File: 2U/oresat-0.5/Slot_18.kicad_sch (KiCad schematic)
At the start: 3 parts

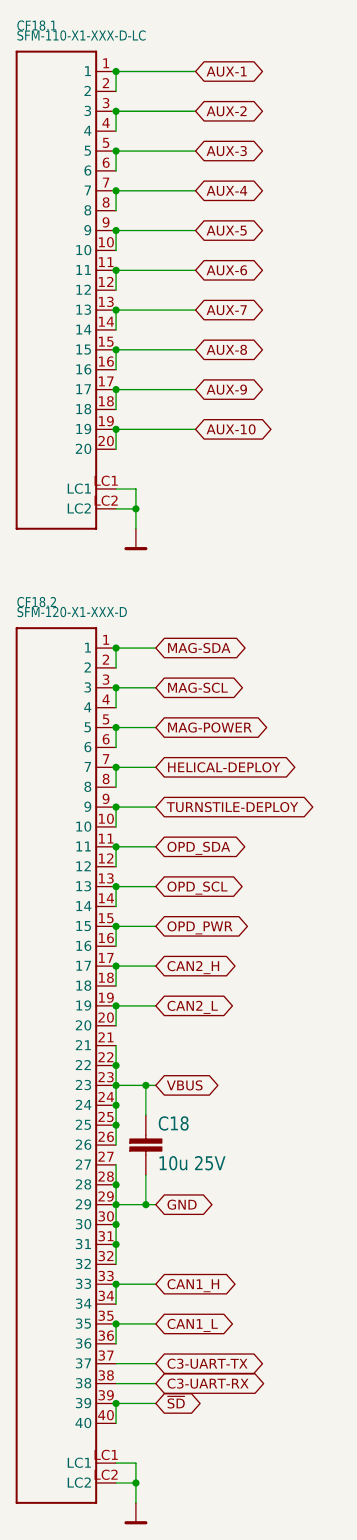
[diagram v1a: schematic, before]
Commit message: Fixed all (most) of the issues from Eagle imports
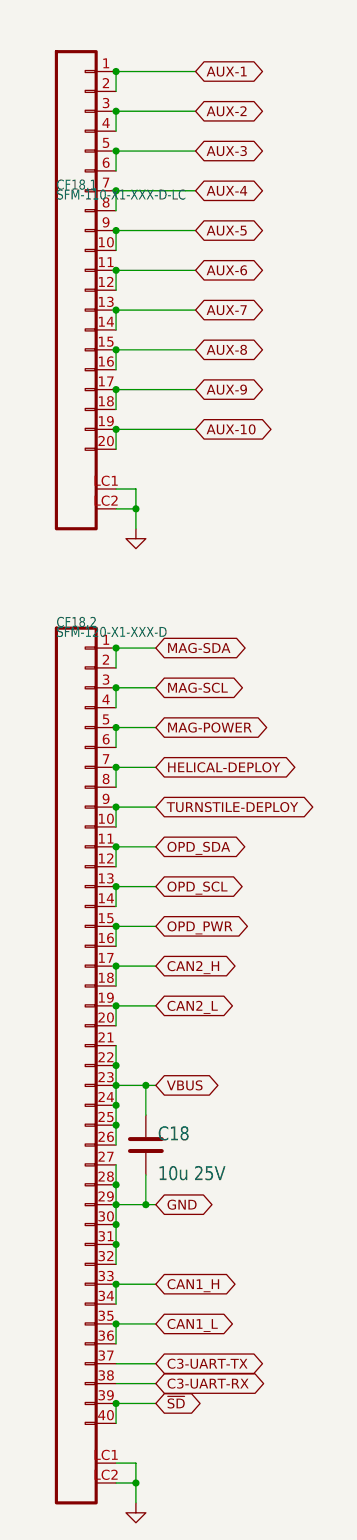
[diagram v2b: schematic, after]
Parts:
- C18: symbol oresat0-1u-backplane-eagle-import:C-EU1206-B -> Device:C
- CF18.1: symbol oresat-backplane-2u-eagle-import:SFM-110-X1-XXX-D-LC -> oresat-connectors:J-SAMTEC-TFM-110-01-L-D-RA
- CF18.2: symbol oresat-backplane-2u-eagle-import:SFM-120-X1-XXX-D -> oresat-connectors:J-SAMTEC-TFM-120-01-L-D-RA

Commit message: Moved entire schematic to single page
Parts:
- removed C18: 10u 25V, Capacitor_SMD:C_1206_3216Metric, symbol Device:C
- removed CF18.1: SFM-110-X1-XXX-D-LC, oresat-connectors:J-SAMTEC-CF-SFM-110-X1-XXX-D-LC, symbol oresat-connectors:J-SAMTEC-TFM-110-01-L-D-RA
- removed CF18.2: SFM-120-X1-XXX-D, oresat-connectors:J-SAMTEC-SFM-120-X1-XXX-D, symbol oresat-connectors:J-SAMTEC-TFM-120-01-L-D-RA
